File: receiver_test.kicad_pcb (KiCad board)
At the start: 2 copper layers, 65 x 61 mm, 126 parts, among them J1 5V, J2 RF_IN, J3 IF_IN, J4 Conn_01x02_Male, J5 Conn_01x02_Male, Q1 MMBT5089, Q2 BC847BS, U1 ADE-1H+, U2 SA612, U3 MCP6D11, U4 FST3253, Y1 28.224 MHz

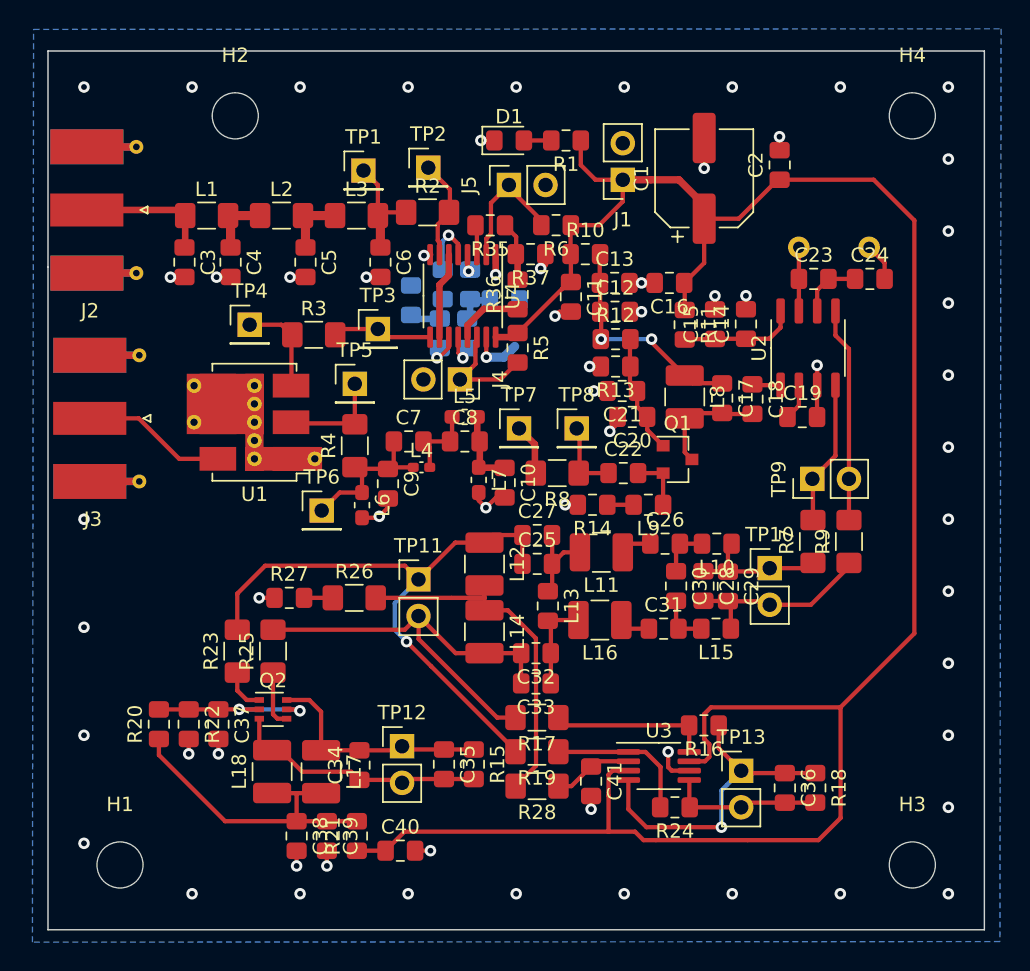
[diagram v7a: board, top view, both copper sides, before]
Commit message: Via stitching removed + Edge Cut resized
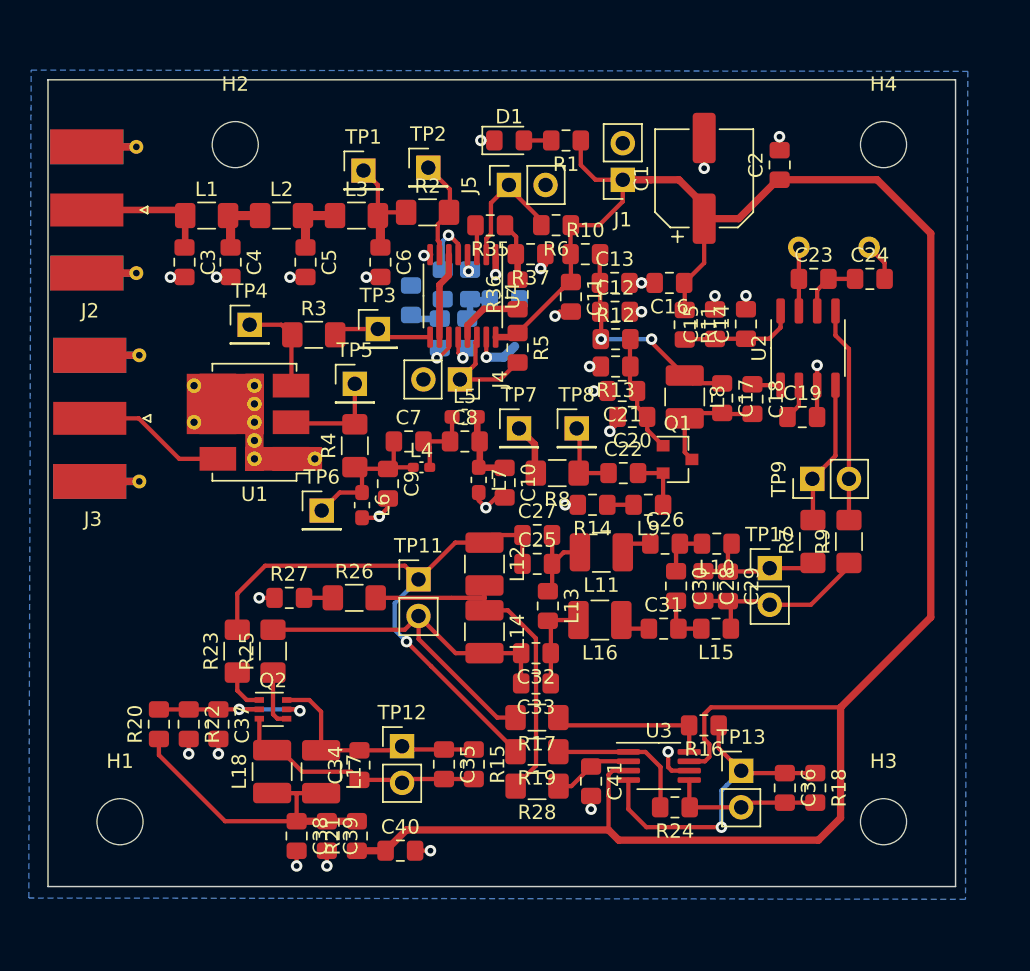
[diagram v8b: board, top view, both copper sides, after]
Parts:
- moved H3 3.61 mm to (93.0, 126.0)
- moved H1 3.00 mm to (40.0, 126.0)
- moved H4 2.83 mm to (93.0, 79.0)
- moved H2 2.00 mm to (48.0, 79.0)
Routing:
- net +5VA: track 151.1 -> 152.2 mm
- net GNDA: vias 62 -> 31
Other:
- board size 65 x 61 mm -> 63 x 56 mm
